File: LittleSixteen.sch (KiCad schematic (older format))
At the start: 13 parts

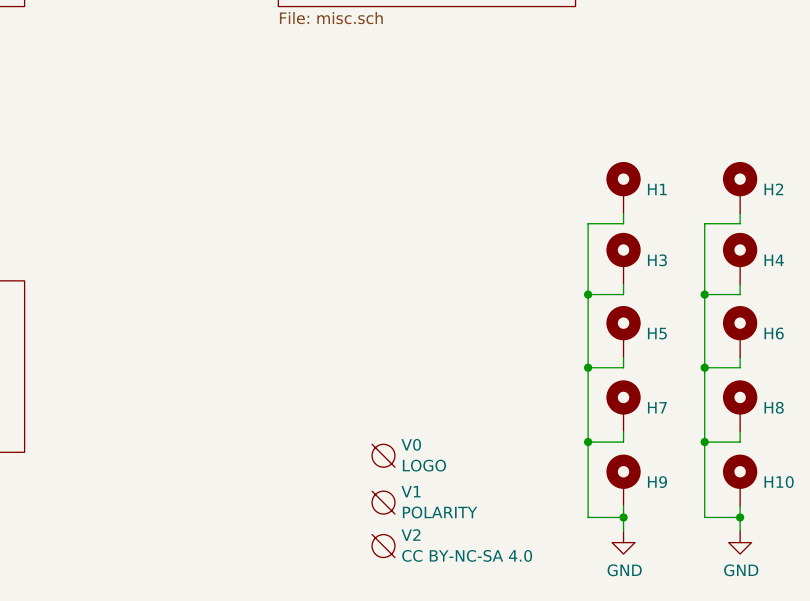
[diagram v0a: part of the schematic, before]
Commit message: Make holes for cart connector metal cover
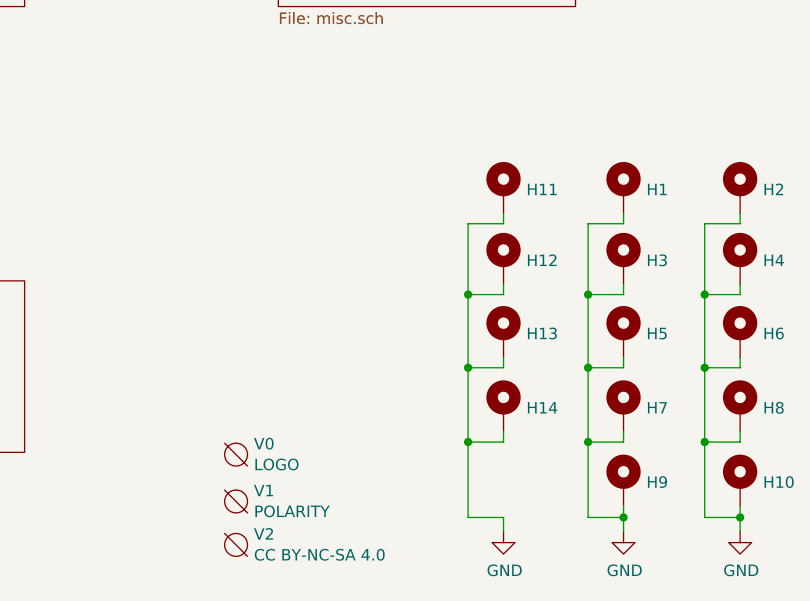
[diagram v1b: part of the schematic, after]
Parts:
- added H11, H12, H13, H14: MountingHole_Pad, MountingHole:MountingHole_2.7mm_Pad, symbol Mechanical:MountingHole_Pad
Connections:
- net GND: now also H11.1, H12.1, H13.1, H14.1
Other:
- moved on the sheet: V0, V1, V2
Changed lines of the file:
@@
 Sheet 1 12
 Title "LittleSixteen"
-Date "2021-11-02"
+Date "2021-11-17"
 Rev "3git"
 Comp "SukkoPera"
@@
 L void:Void V1
 U 1 1 61157949
-P 9270 6100
-F 0 "V1" H 9348 6146 50  0000 L CNN
-F 1 "POLARITY" H 9348 6055 50  0000 L CNN
-F 2 "w_logo:Logo_silk_polarity_external_10x2.8mm" H 9270 6100 50  0001 C CNN
-F 3 "" H 9270 6100 50  0001 C CNN
-	1    9270 6100
+P 8625 6095
+F 0 "V1" H 8703 6141 50  0000 L CNN
+F 1 "POLARITY" H 8703 6050 50  0000 L CNN
+F 2 "w_logo:Logo_silk_polarity_external_10x2.8mm" H 8625 6095 50  0001 C CNN
+F 3 "" H 8625 6095 50  0001 C CNN
+	1    8625 6095
 	1    0    0    -1
 $EndComp
@@
 L void:Void V0
 U 1 1 61145DF1
-P 9270 5895
-F 0 "V0" H 9348 5941 50  0000 L CNN
-F 1 "LOGO" H 9348 5850 50  0000 L CNN
-F 2 "LittleSixteen:Logo" H 9270 5895 50  0001 C CNN
-F 3 "" H 9270 5895 50  0001 C CNN
-	1    9270 5895
+P 8625 5890
+F 0 "V0" H 8703 5936 50  0000 L CNN
+F 1 "LOGO" H 8703 5845 50  0000 L CNN
+F 2 "LittleSixteen:Logo" H 8625 5890 50  0001 C CNN
+F 3 "" H 8625 5890 50  0001 C CNN
+	1    8625 5890
 	1    0    0    -1
 $EndComp
@@
 L void:Void V2
 U 1 1 61992CC0
-P 9270 6290
-F 0 "V2" H 9348 6336 50  0000 L CNN
-F 1 "CC BY-NC-SA 4.0" H 9348 6245 50  0000 L CNN
-F 2 "LittleSixteen:cc_by_nc_sa" H 9270 6290 50  0001 C CNN
-F 3 "" H 9270 6290 50  0001 C CNN
-	1    9270 6290
-	1    0    0    -1
-$EndComp
+P 8625 6285
+F 0 "V2" H 8703 6331 50  0000 L CNN
+F 1 "CC BY-NC-SA 4.0" H 8703 6240 50  0000 L CNN
+F 2 "LittleSixteen:cc_by_nc_sa" H 8625 6285 50  0001 C CNN
+F 3 "" H 8625 6285 50  0001 C CNN
+	1    8625 6285
+	1    0    0    -1
+$EndComp
+$Comp
+L Mechanical:MountingHole_Pad H11
+U 1 1 61A81AD7
+P 9795 4735
+F 0 "H11" H 9895 4738 50  0000 L CNN
+F 1 "MountingHole_Pad" H 9895 4693 50  0001 L CNN
+F 2 "MountingHole:MountingHole_2.7mm_Pad" H 9795 4735 50  0001 C CNN
+F 3 "~" H 9795 4735 50  0001 C CNN
+	1    9795 4735
+	1    0    0    -1
+$EndComp
+$Comp
+L Mechanical:MountingHole_Pad H12
+U 1 1 61A81BB9
+P 9795 5045
+F 0 "H12" H 9895 5048 50  0000 L CNN
+F 1 "MountingHole_Pad" H 9895 5003 50  0001 L CNN
+F 2 "MountingHole:MountingHole_2.7mm_Pad" H 9795 5045 50  0001 C CNN
+F 3 "~" H 9795 5045 50  0001 C CNN
+	1    9795 5045
+	1    0    0    -1
+$EndComp
+$Comp
+L Mechanical:MountingHole_Pad H13
+U 1 1 61A81BC3
+P 9795 5365
+F 0 "H13" H 9895 5368 50  0000 L CNN
+F 1 "MountingHole_Pad" H 9895 5323 50  0001 L CNN
+F 2 "MountingHole:MountingHole_2.7mm_Pad" H 9795 5365 50  0001 C CNN
+F 3 "~" H 9795 5365 50  0001 C CNN
+	1    9795 5365
+	1    0    0    -1
+$EndComp
+$Comp
+L Mechanical:MountingHole_Pad H14
+U 1 1 61A81BCD
+P 9795 5690
+F 0 "H14" H 9895 5693 50  0000 L CNN
+F 1 "MountingHole_Pad" H 9895 5648 50  0001 L CNN
+F 2 "MountingHole:MountingHole_2.7mm_Pad" H 9795 5690 50  0001 C CNN
+F 3 "~" H 9795 5690 50  0001 C CNN
+	1    9795 5690
+	1    0    0    -1
+$EndComp
+Wire Wire Line
+	9640 6165 9795 6165
+Wire Wire Line
+	9795 6165 9795 6225
+$Comp
+L power:GND #PWR07
+U 1 1 61A81BE3
+P 9795 6225
+F 0 "#PWR07" H 9795 5975 50  0001 C CNN
+F 1 "GND" H 9800 6052 50  0000 C CNN
+F 2 "" H 9795 6225 50  0001 C CNN
+F 3 "" H 9795 6225 50  0001 C CNN
+	1    9795 6225
+	1    0    0    -1
+$EndComp
+Wire Wire Line
+	9795 5790 9795 5835
+Wire Wire Line
+	9795 5835 9640 5835
+Connection ~ 9640 5835
+Wire Wire Line
+	9640 5835 9640 6165
+Wire Wire Line
+	9795 5465 9795 5510
+Wire Wire Line
+	9795 5510 9640 5510
+Connection ~ 9640 5510
+Wire Wire Line
+	9640 5510 9640 5835
+Wire Wire Line
+	9795 5145 9795 5190
+Wire Wire Line
+	9795 5190 9640 5190
+Connection ~ 9640 5190
+Wire Wire Line
+	9640 5190 9640 5510
+Wire Wire Line
+	9795 4835 9795 4880
+Wire Wire Line
+	9795 4880 9640 4880
+Wire Wire Line
+	9640 4880 9640 5190
 $EndSCHEMATC

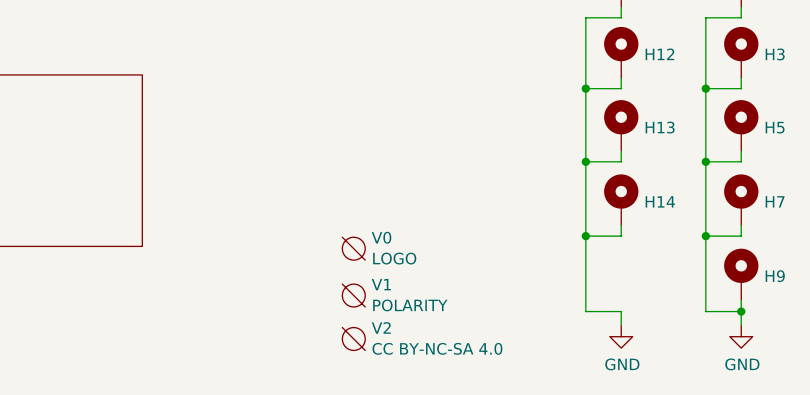
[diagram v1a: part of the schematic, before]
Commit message: Switch to C64-style Power Connector
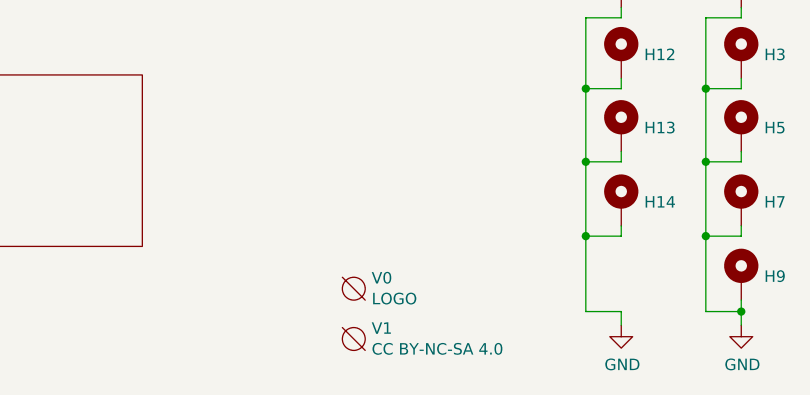
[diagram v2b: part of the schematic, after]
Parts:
- removed V1: POLARITY, w_logo:Logo_silk_polarity_external_10x2.8mm, symbol void:Void
- renumbered V2 to V1
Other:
- moved on the sheet: V0
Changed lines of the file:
@@
 	10675 4880 10675 5190
 $Comp
-L void:Void V1
-U 1 1 61157949
-P 8625 6095
-F 0 "V1" H 8703 6141 50  0000 L CNN
-F 1 "POLARITY" H 8703 6050 50  0000 L CNN
-F 2 "w_logo:Logo_silk_polarity_external_10x2.8mm" H 8625 6095 50  0001 C CNN
-F 3 "" H 8625 6095 50  0001 C CNN
-	1    8625 6095
+L void:Void V0
+U 1 1 61145DF1
+P 8625 6065
+F 0 "V0" H 8703 6111 50  0000 L CNN
+F 1 "LOGO" H 8703 6020 50  0000 L CNN
+F 2 "LittleSixteen:Logo" H 8625 6065 50  0001 C CNN
+F 3 "" H 8625 6065 50  0001 C CNN
+	1    8625 6065
 	1    0    0    -1
 $EndComp
 $Comp
-L void:Void V0
-U 1 1 61145DF1
-P 8625 5890
-F 0 "V0" H 8703 5936 50  0000 L CNN
-F 1 "LOGO" H 8703 5845 50  0000 L CNN
-F 2 "LittleSixteen:Logo" H 8625 5890 50  0001 C CNN
-F 3 "" H 8625 5890 50  0001 C CNN
-	1    8625 5890
-	1    0    0    -1
-$EndComp
-$Comp
-L void:Void V2
+L void:Void V1
 U 1 1 61992CC0
 P 8625 6285
-F 0 "V2" H 8703 6331 50  0000 L CNN
+F 0 "V1" H 8703 6331 50  0000 L CNN
 F 1 "CC BY-NC-SA 4.0" H 8703 6240 50  0000 L CNN
 F 2 "LittleSixteen:cc_by_nc_sa" H 8625 6285 50  0001 C CNN

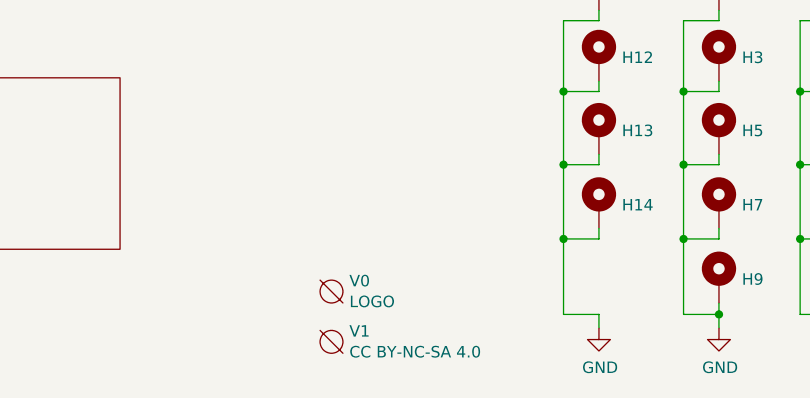
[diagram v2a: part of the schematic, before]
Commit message: Add PCBWay logo
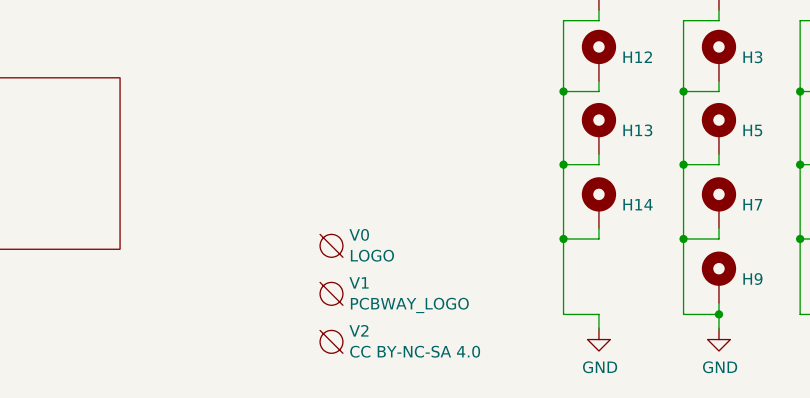
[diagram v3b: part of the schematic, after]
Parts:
- added V1: PCBWAY_LOGO, LittleSixteen:pcbway, symbol void:Void
- renumbered V1 to V2
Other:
- moved on the sheet: V0
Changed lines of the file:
@@
 L void:Void V0
 U 1 1 61145DF1
-P 8625 6065
-F 0 "V0" H 8703 6111 50  0000 L CNN
-F 1 "LOGO" H 8703 6020 50  0000 L CNN
-F 2 "LittleSixteen:Logo" H 8625 6065 50  0001 C CNN
-F 3 "" H 8625 6065 50  0001 C CNN
-	1    8625 6065
+P 8625 5865
+F 0 "V0" H 8703 5911 50  0000 L CNN
+F 1 "LOGO" H 8703 5820 50  0000 L CNN
+F 2 "LittleSixteen:Logo" H 8625 5865 50  0001 C CNN
+F 3 "" H 8625 5865 50  0001 C CNN
+	1    8625 5865
 	1    0    0    -1
 $EndComp
 $Comp
-L void:Void V1
+L void:Void V2
 U 1 1 61992CC0
 P 8625 6285
-F 0 "V1" H 8703 6331 50  0000 L CNN
+F 0 "V2" H 8703 6331 50  0000 L CNN
 F 1 "CC BY-NC-SA 4.0" H 8703 6240 50  0000 L CNN
 F 2 "LittleSixteen:cc_by_nc_sa" H 8625 6285 50  0001 C CNN
@@
 Wire Wire Line
 	9640 4880 9640 5190
+$Comp
+L void:Void V1
+U 1 1 63408BAA
+P 8625 6075
+F 0 "V1" H 8703 6121 50  0000 L CNN
+F 1 "PCBWAY_LOGO" H 8703 6030 50  0000 L CNN
+F 2 "LittleSixteen:pcbway" H 8625 6075 50  0001 C CNN
+F 3 "" H 8625 6075 50  0001 C CNN
+	1    8625 6075
+	1    0    0    -1
+$EndComp
 $EndSCHEMATC

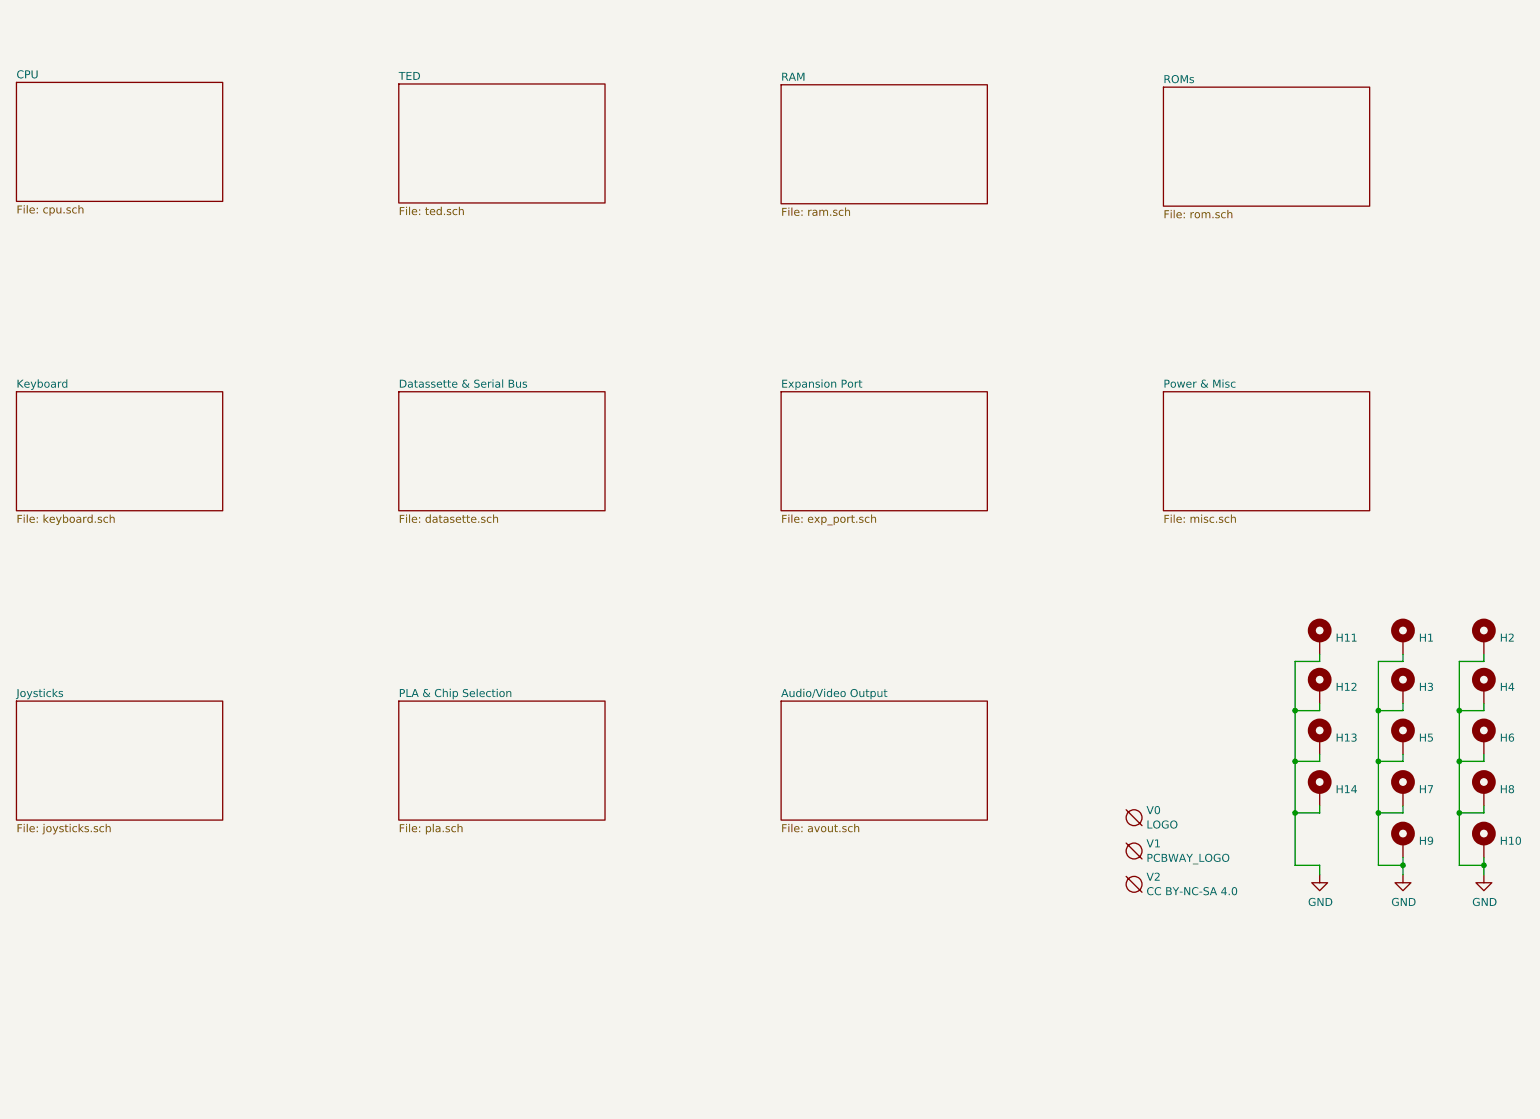
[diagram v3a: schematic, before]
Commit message: Add userport schematics and enlarge board
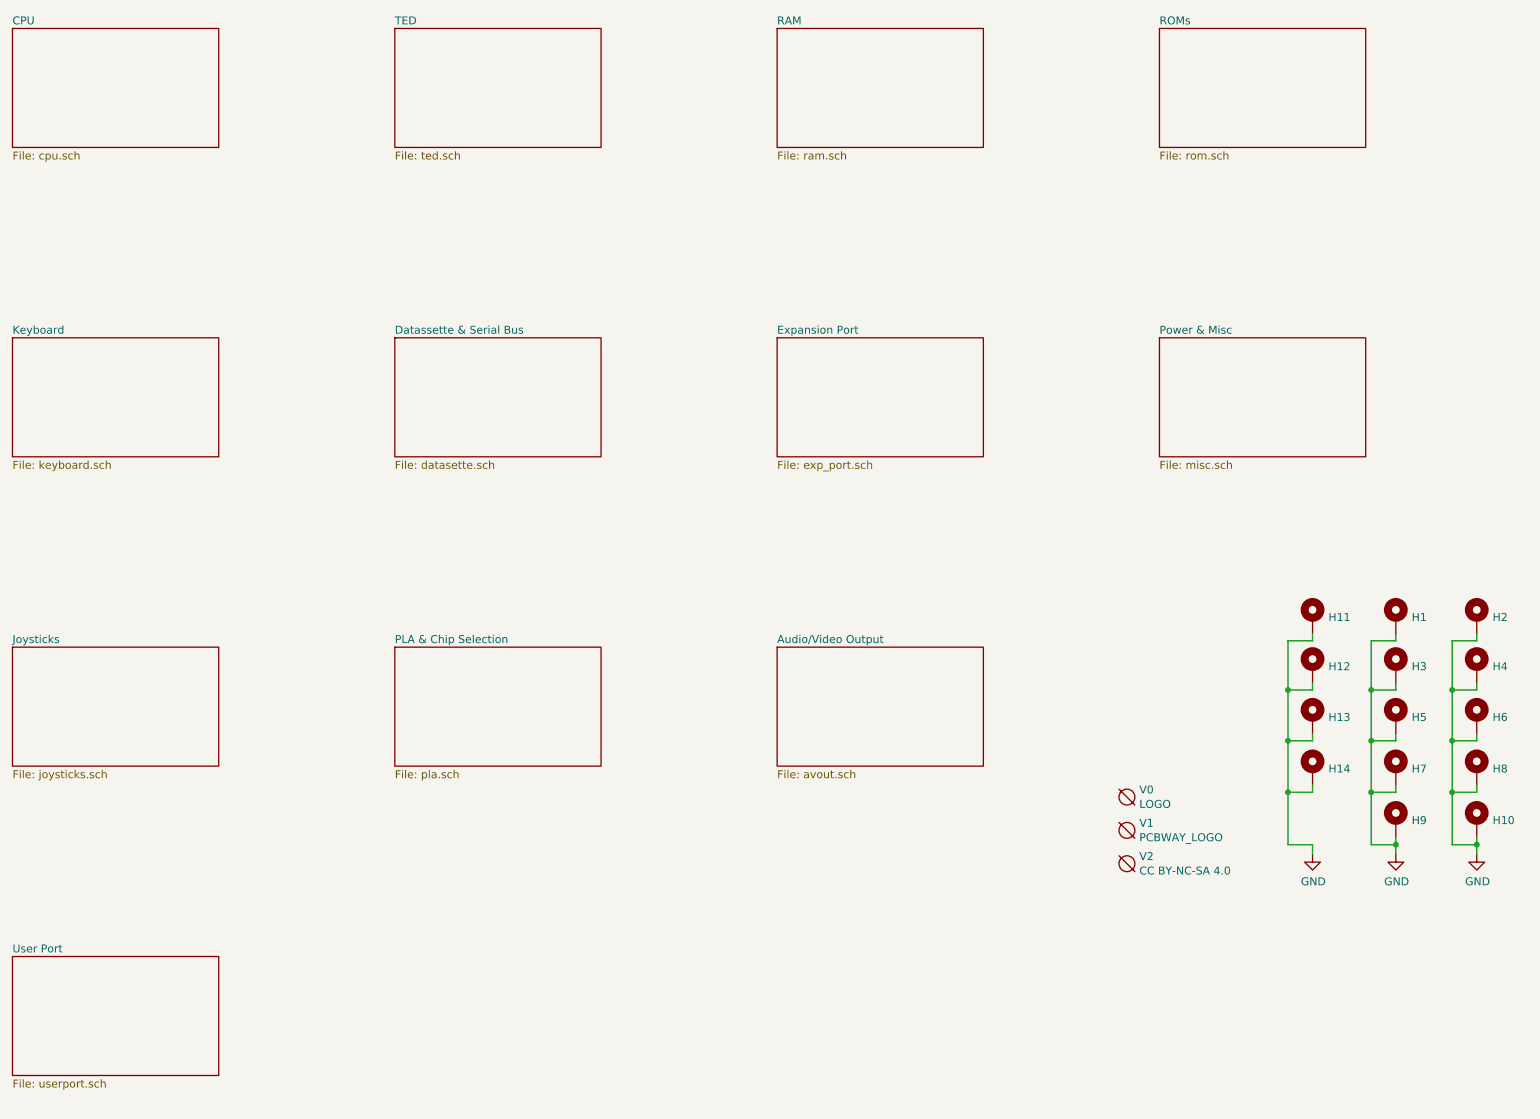
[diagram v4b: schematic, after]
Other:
- moved on the sheet: H1, H10, H11, H12, H13, H14, H2, H3, H4, H5, H6, H7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

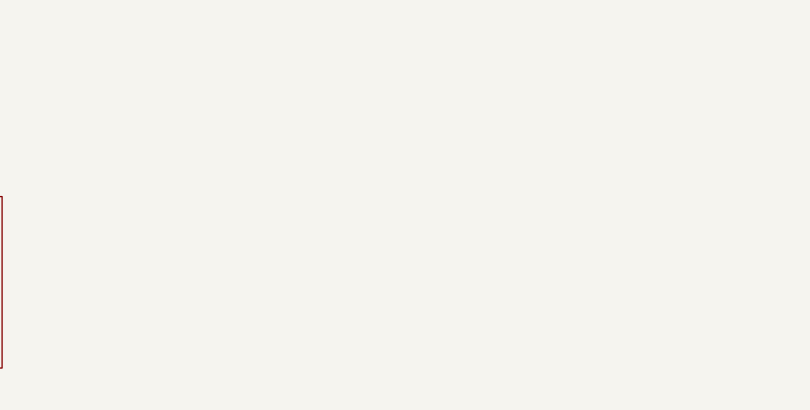
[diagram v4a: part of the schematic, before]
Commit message: Add SID schematics
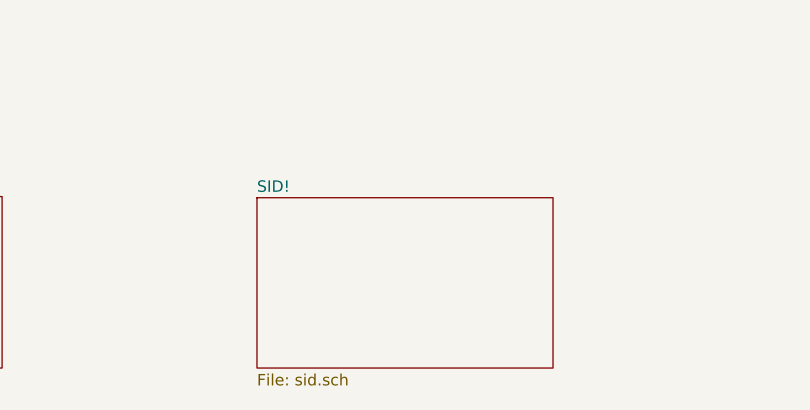
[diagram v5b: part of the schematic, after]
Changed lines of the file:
@@
 $Descr A4 11693 8268
 encoding utf-8
-Sheet 1 13
+Sheet 1 14
 Title "LittleSixteen"
 Date "2023-02-15"
@@
 Comp "SukkoPera"
 Comment1 "Licensed under CC BY-NC-SA 4.0"
-Comment2 "WARNING: These schematics might contain errors!"
+Comment2 ""
 Comment3 ""
 Comment4 ""
@@
 F1 "userport.sch" 50
 $EndSheet
+$Sheet
+S 3970 6745 1295 745
+U 64A6E6F3
+F0 "SID!" 50
+F1 "sid.sch" 50
+$EndSheet
 $EndSCHEMATC
